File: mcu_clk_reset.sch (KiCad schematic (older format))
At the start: 52 parts

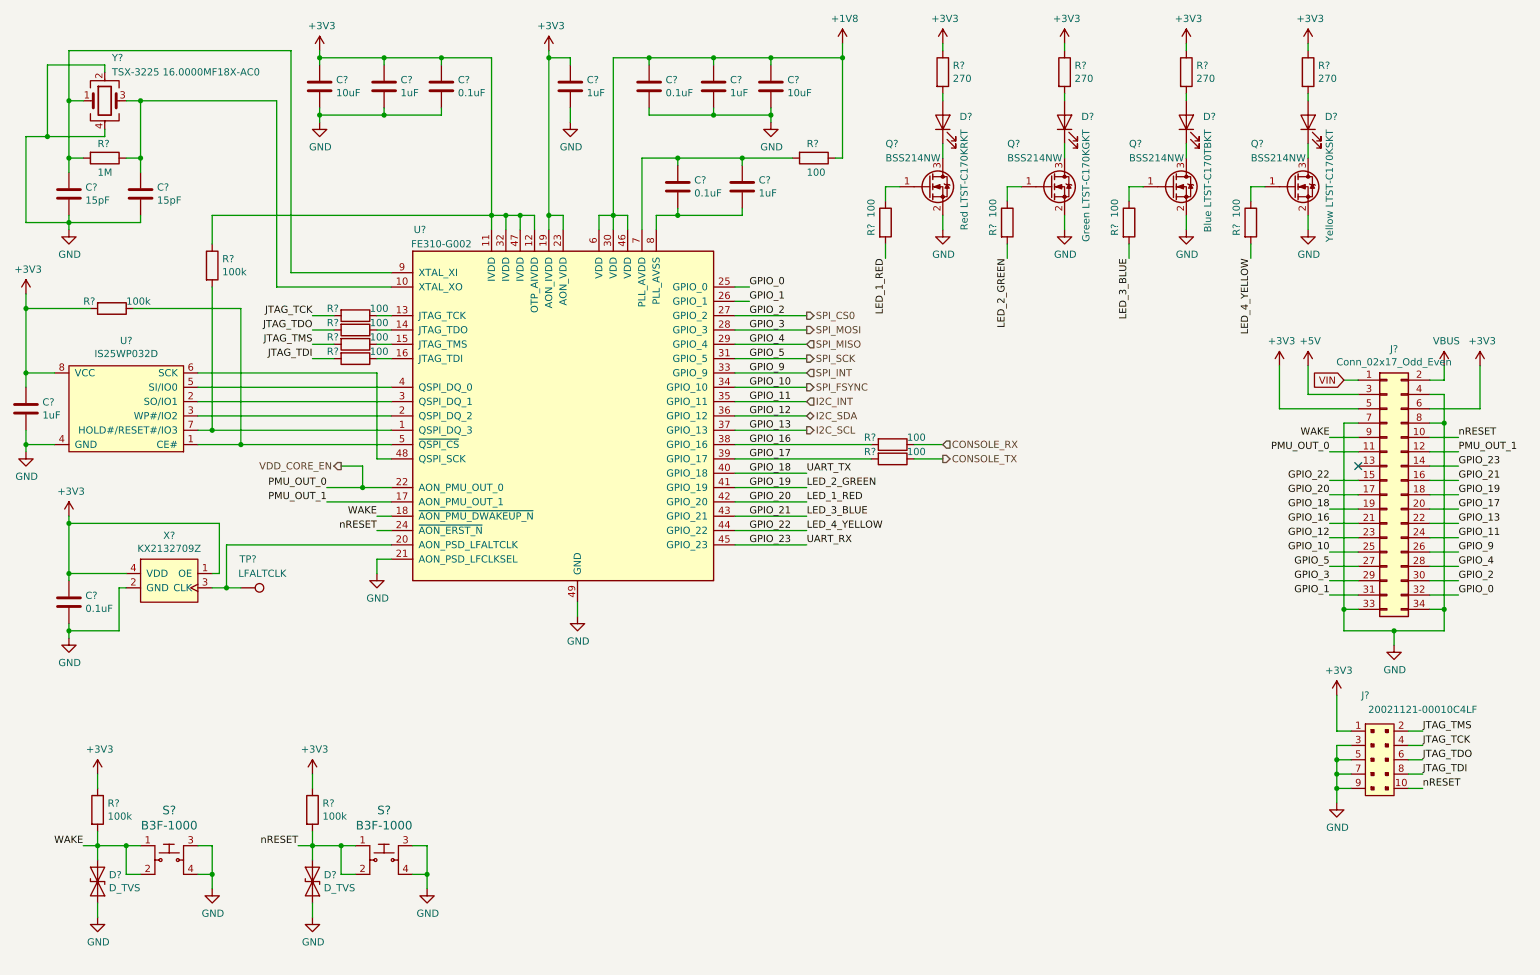
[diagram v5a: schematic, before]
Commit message: Moved some schematics around, no real changes
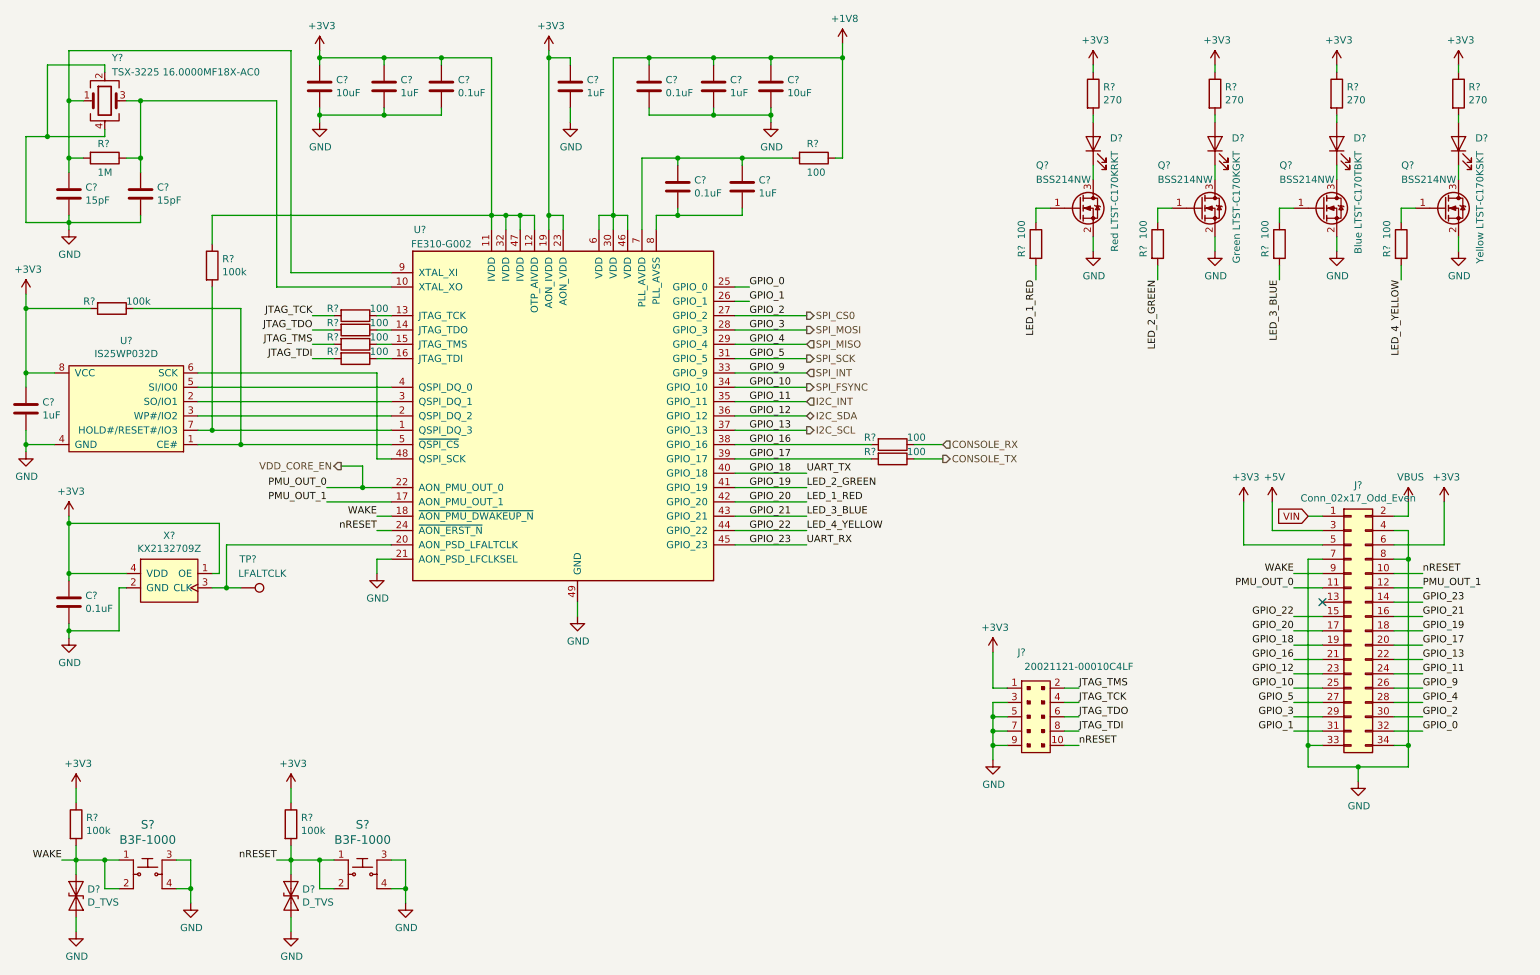
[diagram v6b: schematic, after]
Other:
- moved on the sheet: D?, J?, Q?, R?, S?

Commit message: Add ERC fixes, mostly PWR_FLAGs
Also, fixed MCP1726 symbol.
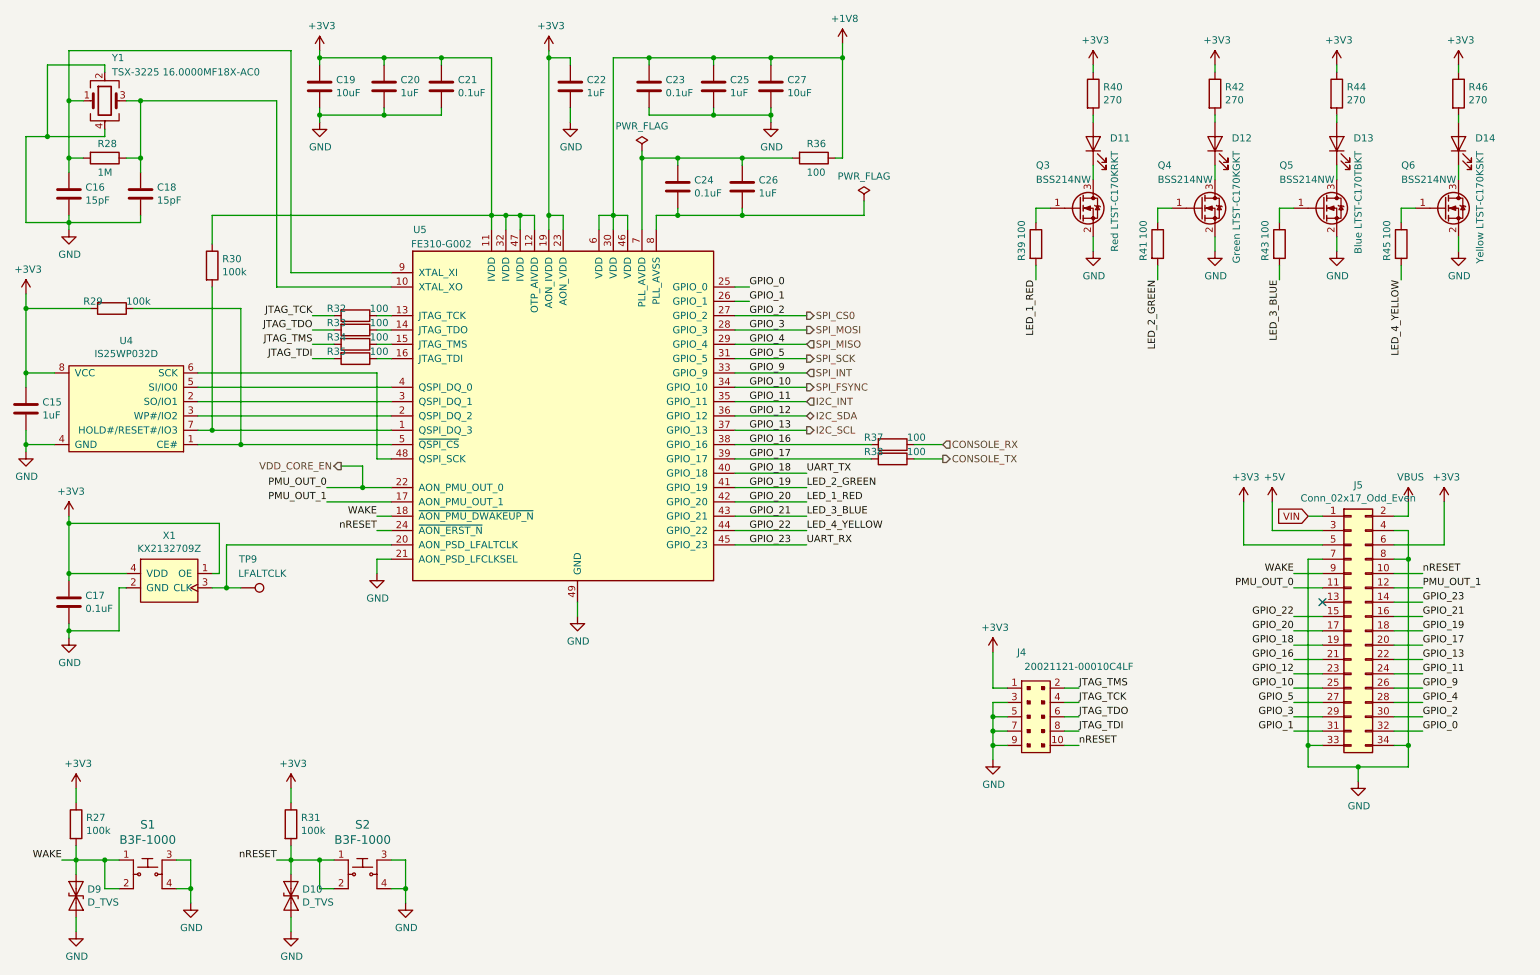
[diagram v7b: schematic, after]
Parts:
- gave numbers to parts that had none: 52

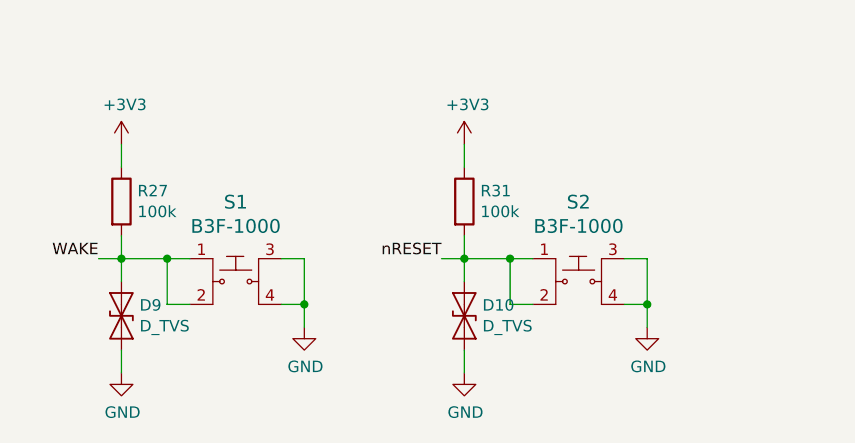
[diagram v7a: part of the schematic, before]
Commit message: Assigned footprints, generated netlist
I can already see some footprints issues. Eg. the switches have to be
changed to the SMT version. There are some silkscreen issues in custom
oscillator footprints. Otherwise looks promising :)
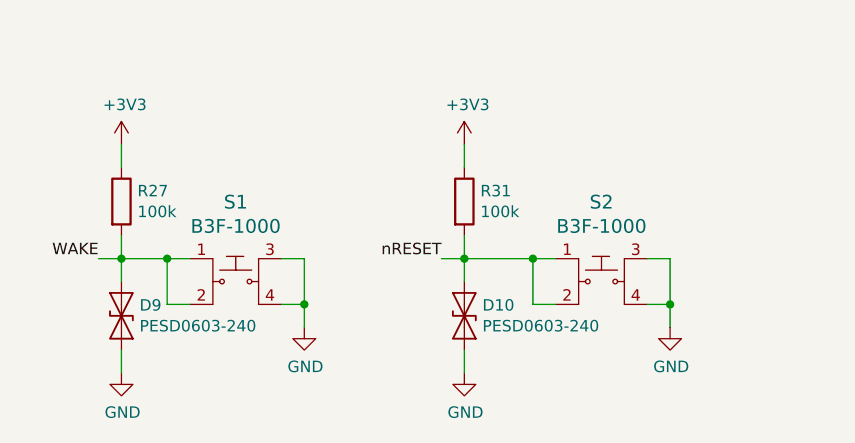
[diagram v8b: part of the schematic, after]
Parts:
- C15, C16, C17, C18, C19, C20, C21, C22, C23, C24, C25, C26, C27: footprint (none) -> Capacitor_SMD:C_0805_2012Metric_Pad1.15x1.40mm_HandSolder
- D10, D9: value D_TVS -> PESD0603-240; footprint (none) -> Diode_SMD:D_0603_1608Metric_Pad1.05x0.95mm_HandSolder
- D11, D12, D13, D14: footprint (none) -> LED_SMD:LED_0805_2012Metric_Pad1.15x1.40mm_HandSolder
- J5: footprint (none) -> Connector_PinHeader_2.54mm:PinHeader_2x17_P2.54mm_Vertical_SMD
- R27, R28, R29, R30, R31, R32, R33, R34, R35, R36, R37, R38, R39, R40, R41, R42, R43, R44, R45, R46: footprint (none) -> Resistor_SMD:R_0805_2012Metric_Pad1.15x1.40mm_HandSolder
- TP9: footprint (none) -> TestPoint:TestPoint_Pad_D1.5mm
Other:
- moved on the sheet: S2
